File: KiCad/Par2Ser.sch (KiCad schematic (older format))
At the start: 40 parts, among them J1 DB25_Male, J2 USB_C_Receptacle_USB2.0, J3 Conn_02x05_Odd_Even, U1 LC4064V-75TN48C, U2 FT240XS-R, U3 TLV75533PDBVR

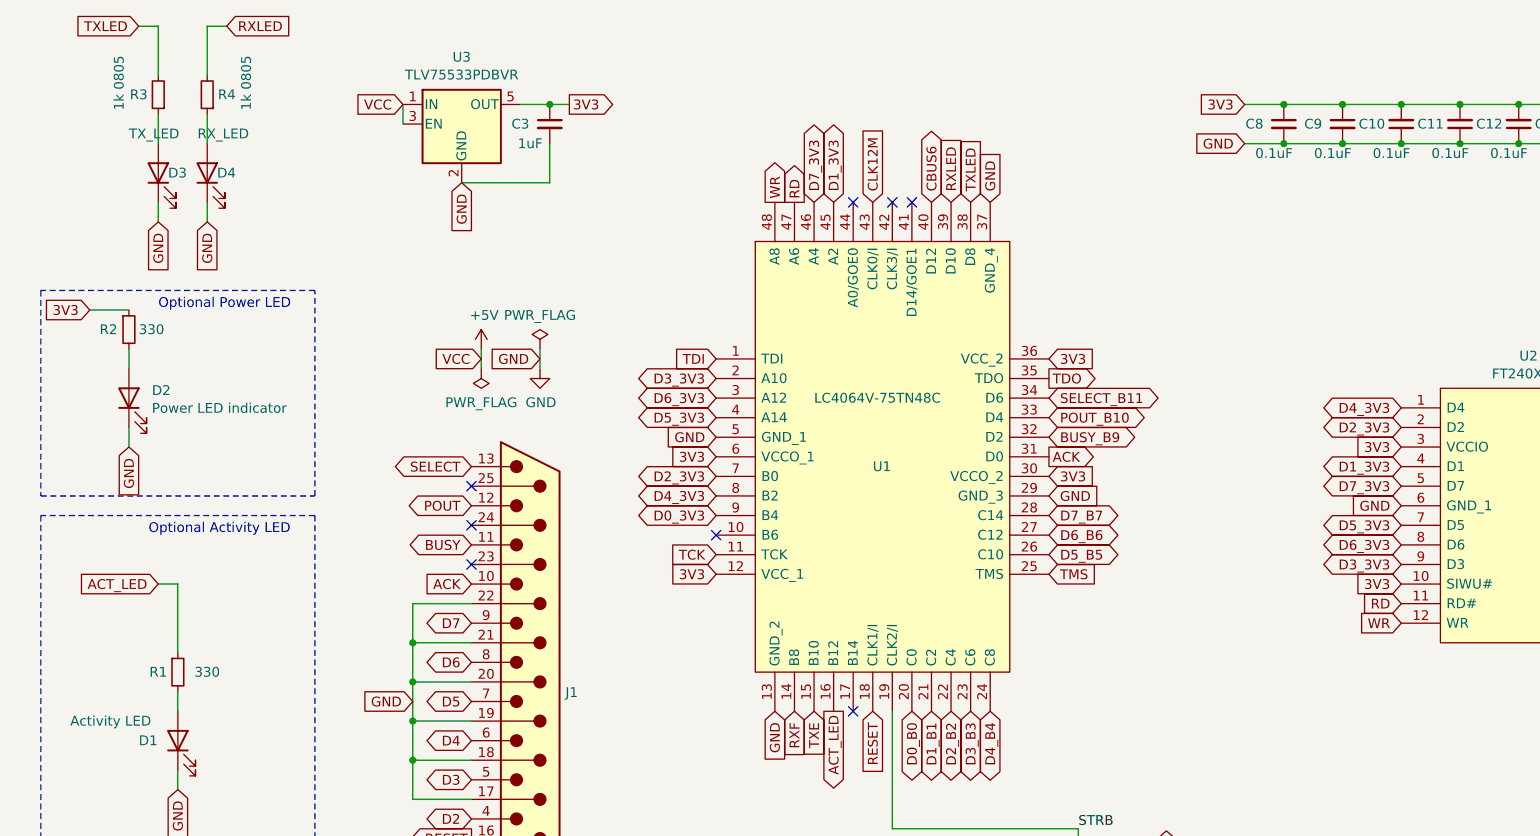
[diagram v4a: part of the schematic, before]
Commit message: Change Ohm values on R1 (1k for Yellow ACT LED) and R2 (10k for Power indicator LED) tested and verified suitable levels of glow
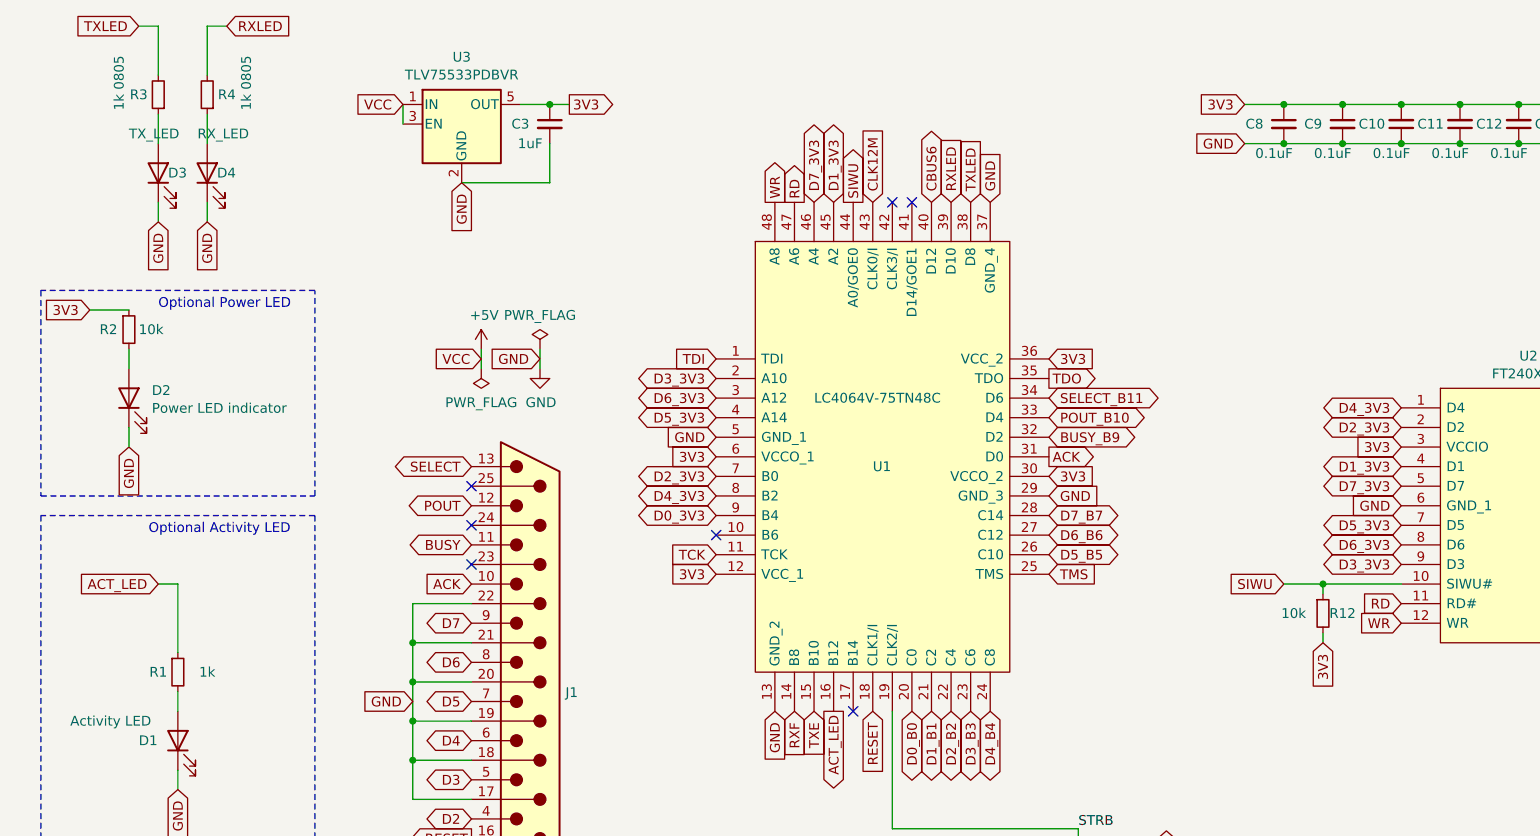
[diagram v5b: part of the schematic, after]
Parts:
- added R12: 10k, Resistor_SMD:R_0603_1608Metric_Pad0.98x0.95mm_HandSolder, symbol Device:R_Small
- R1: value 330 -> 1k
- R2: value 330 -> 10k
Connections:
- net 3V3: now also R12.2; no longer U2.10 (SIWU#)
- net SIWU: now reaches U1.44 (A0/GOE0)
- net SIWU: now also U2.10 (SIWU#), R12.1
- no-connect marks 18 -> 17
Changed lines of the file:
@@
 P 2000 2300
 F 0 "R2" H 1850 2300 50  0000 L CNN
-F 1 "330" H 2050 2300 50  0000 L CNN
+F 1 "10k" H 2050 2300 50  0000 L CNN
 F 2 "Resistor_SMD:R_0805_2012Metric_Pad1.20x1.40mm_HandSolder" H 2000 2300 50  0001 C CNN
 F 3 "~" H 2000 2300 50  0001 C CNN
@@
 P 2250 4050
 F 0 "R1" H 2150 4050 50  0000 C CNN
-F 1 "330" H 2400 4050 50  0000 C CNN
+F 1 "1k" H 2400 4050 50  0000 C CNN
 F 2 "Resistor_SMD:R_0805_2012Metric_Pad1.20x1.40mm_HandSolder" H 2250 4050 50  0001 C CNN
 F 3 "~" H 2250 4050 50  0001 C CNN
@@
 Text GLabel 5800 1650 1    50   Input ~ 0
 CLK12M
-Text GLabel 8500 3600 0    50   Input ~ 0
+Text GLabel 8100 3900 3    50   Input ~ 0
 3V3
 Text GLabel 9800 3500 2    50   Input ~ 0
@@
 Wire Wire Line
 	7700 1350 7900 1350
-NoConn ~ 5700 1650
 NoConn ~ 5000 3350
 NoConn ~ 6000 1650
@@
 $EndComp
 NoConn ~ 5900 1650
+$Comp
+L Device:R_Small R12
+U 1 1 6A2FCD79
+P 8100 3750
+F 0 "R12" H 8200 3750 50  0000 C CNN
+F 1 "10k" H 7950 3750 50  0000 C CNN
+F 2 "Resistor_SMD:R_0603_1608Metric_Pad0.98x0.95mm_HandSolder" H 8100 3750 50  0001 C CNN
+F 3 "~" H 8100 3750 50  0001 C CNN
+	1    8100 3750
+	1    0    0    -1
+$EndComp
+Wire Wire Line
+	7900 3600 8100 3600
+Wire Wire Line
+	8100 3600 8100 3650
+Connection ~ 8100 3600
+Wire Wire Line
+	8100 3600 8500 3600
+Wire Wire Line
+	8100 3850 8100 3900
+Text GLabel 7900 3600 0    50   Input ~ 0
+SIWU
+Text GLabel 5700 1650 1    50   Output ~ 0
+SIWU
 $EndSCHEMATC
